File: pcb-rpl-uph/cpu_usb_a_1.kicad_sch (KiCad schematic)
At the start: 1 part, among them U5 RPL_UPH_FCBGA1744

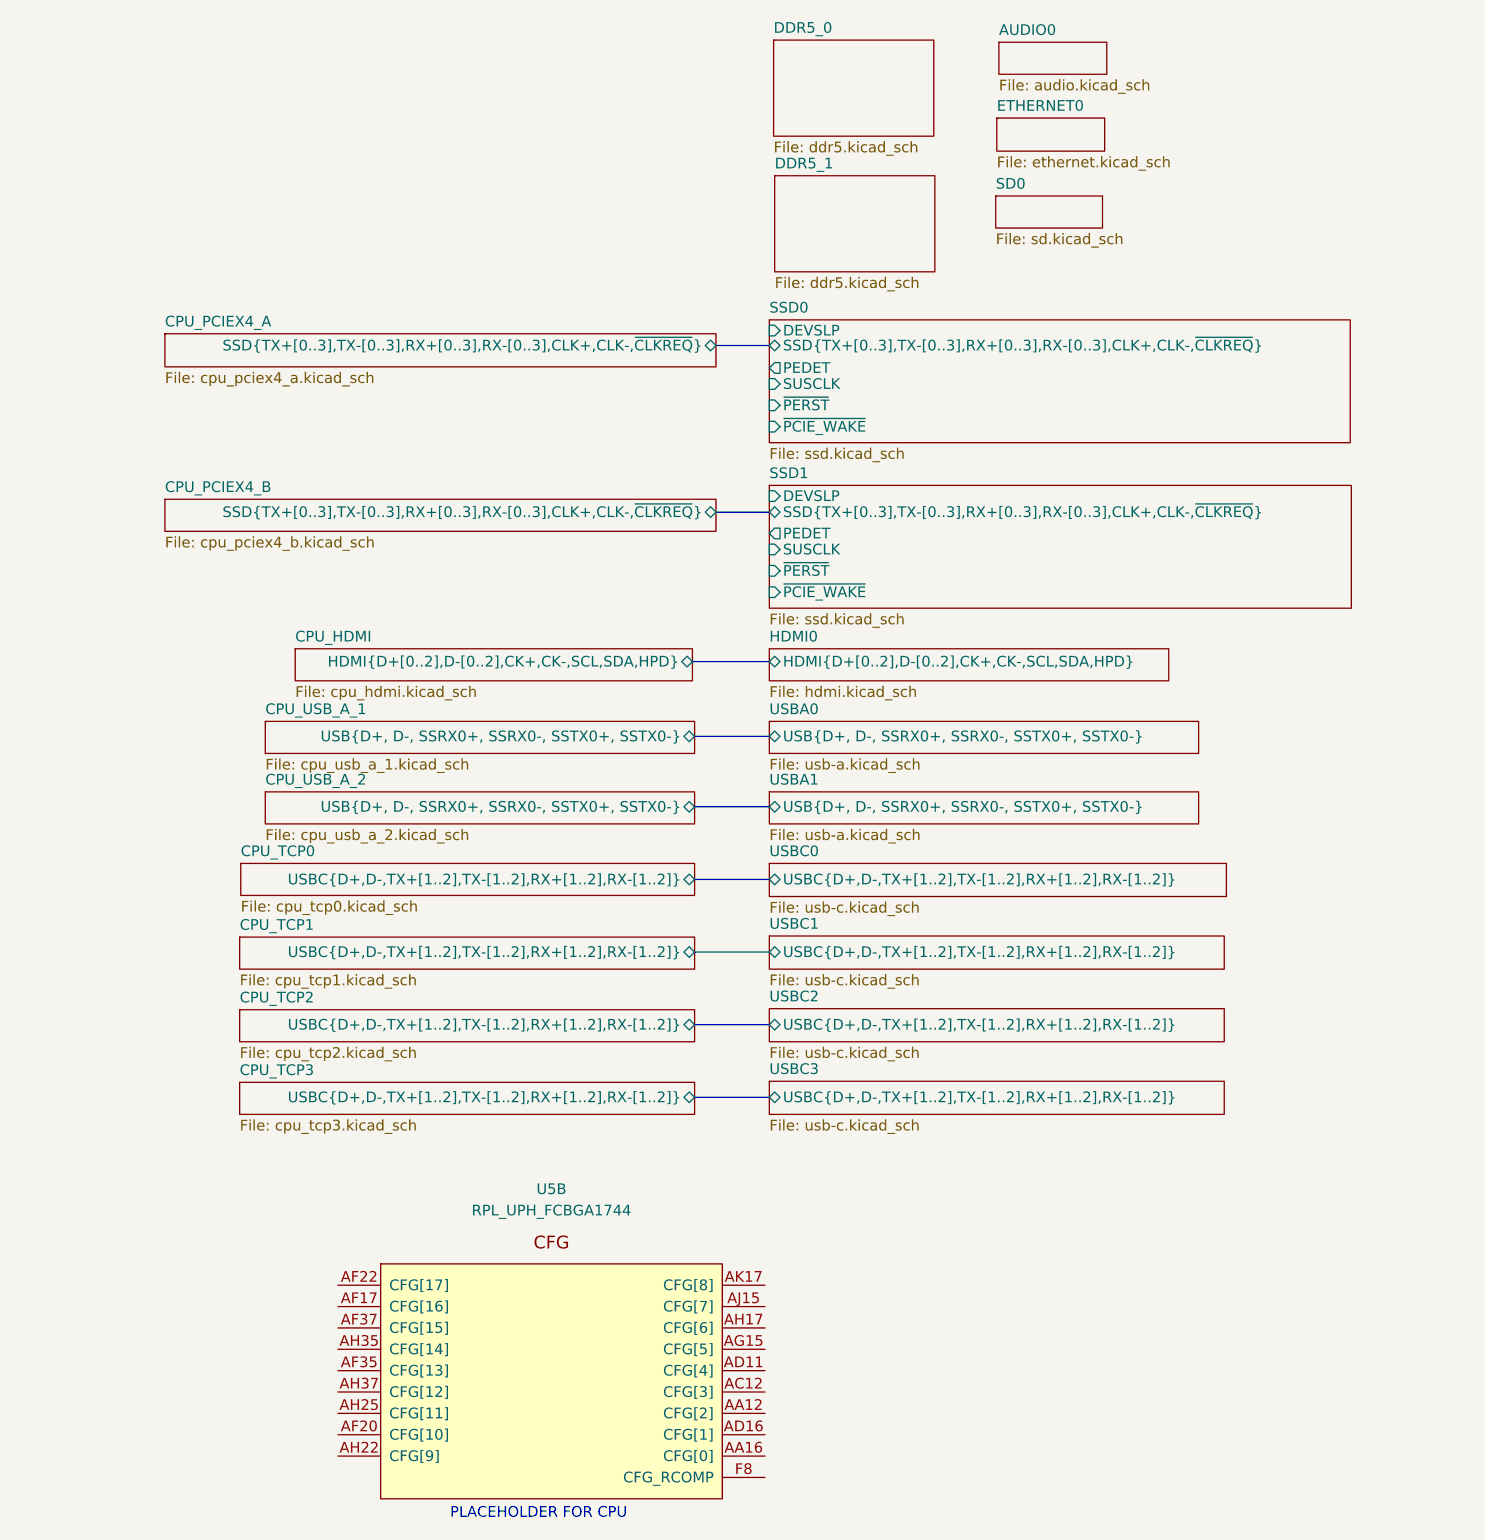
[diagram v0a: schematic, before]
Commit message: Connect USB-A and USB-C data
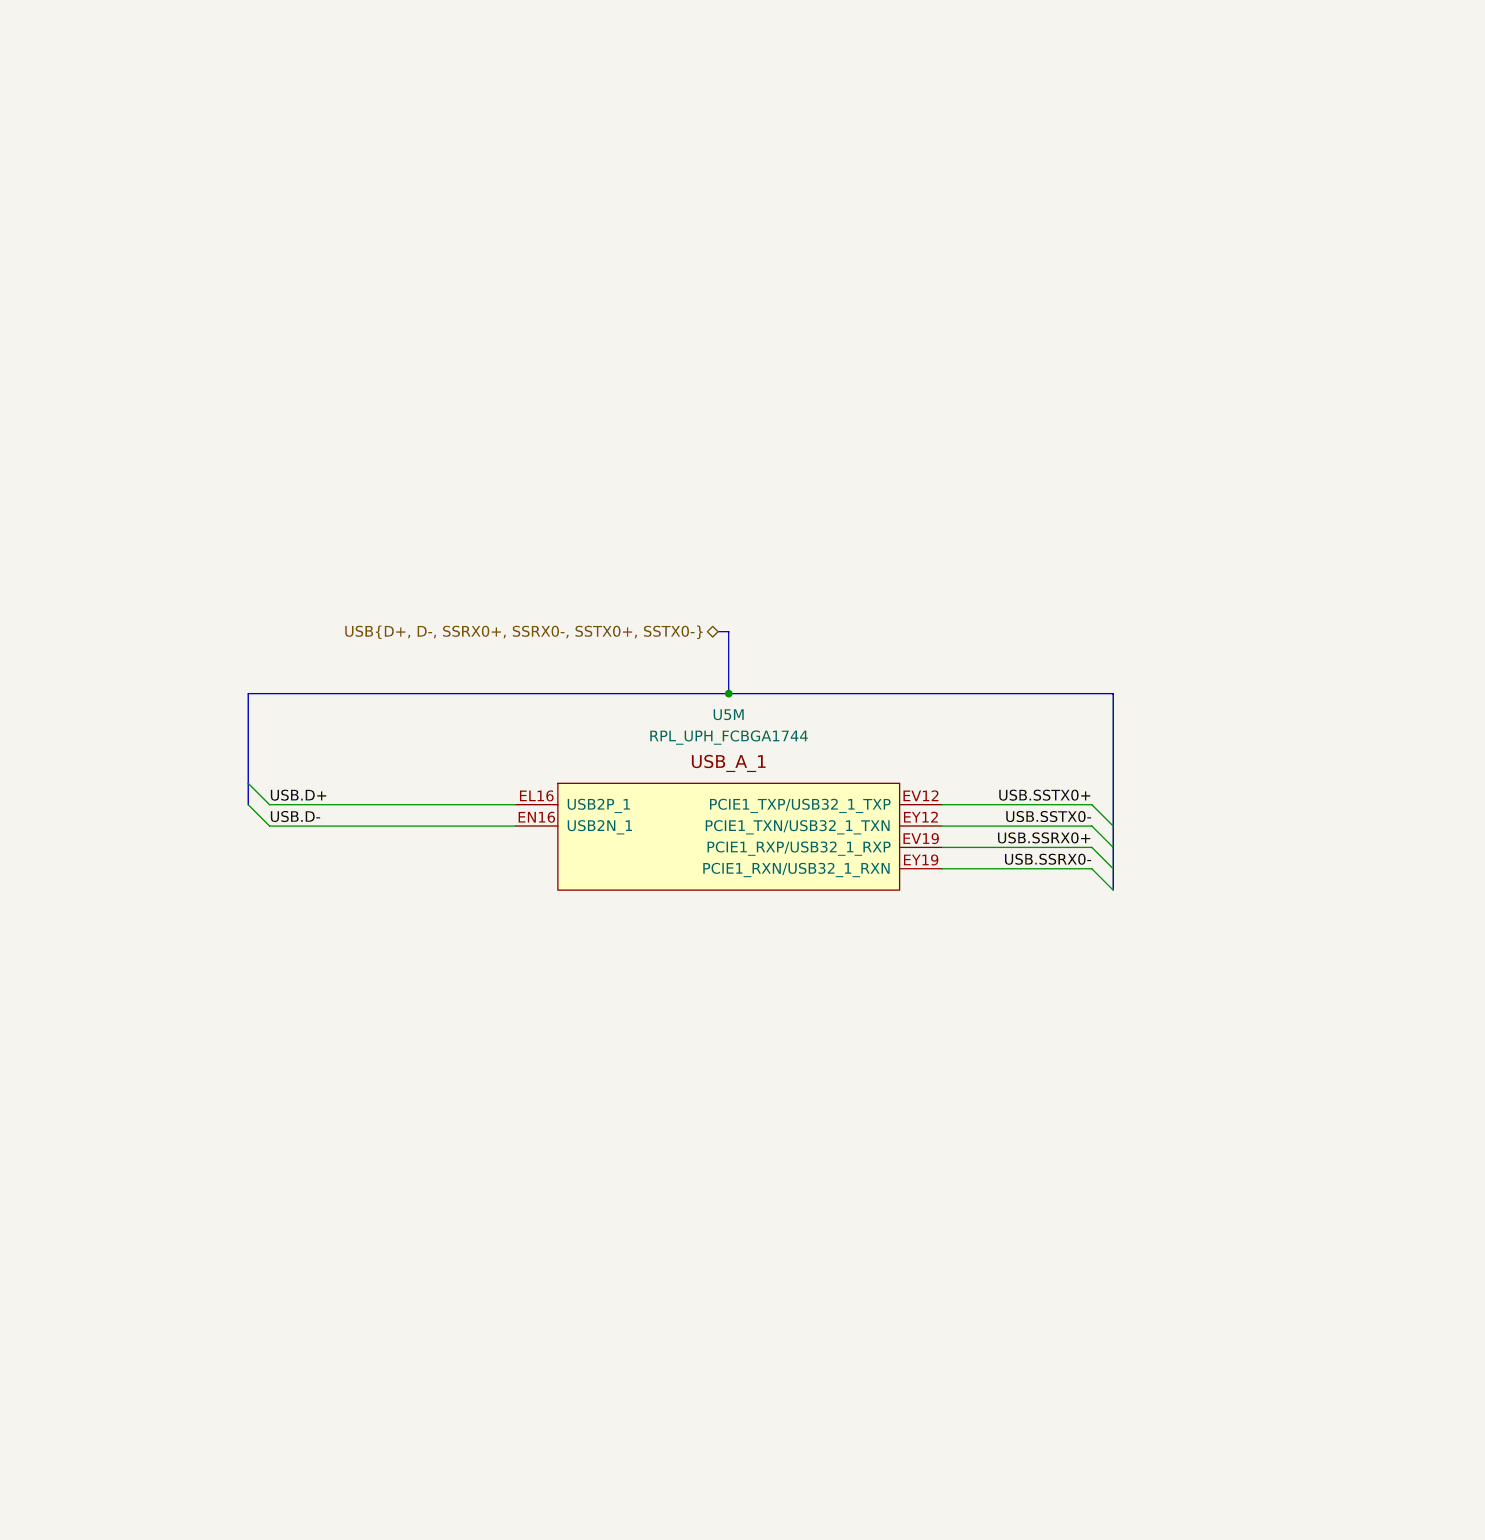
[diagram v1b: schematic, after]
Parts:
- removed U5: RPL_UPH_FCBGA1744, local:RPL_UPH_FCBGA1744, symbol local:RPL_UPH_FCBGA1744
- added U5: RPL_UPH_FCBGA1744, symbol local:RPL_UPH_FCBGA1744
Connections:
- new net USB.D+: U5.EL16 (USB2P_1)
- new net USB.D-: U5.EN16 (USB2N_1)
- new net USB.SSRX0+: U5.EV19 (PCIE1_RXP/USB32_1_RXP)
- new net USB.SSRX0-: U5.EY19 (PCIE1_RXN/USB32_1_RXN)
- new net USB.SSTX0+: U5.EV12 (PCIE1_TXP/USB32_1_TXP)
- new net USB.SSTX0-: U5.EY12 (PCIE1_TXN/USB32_1_TXN)
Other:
- removed sheet AUDIO0
- removed sheet CPU_HDMI
- removed sheet CPU_PCIEX4_A
- removed sheet CPU_PCIEX4_B
- removed sheet CPU_TCP0
- removed sheet CPU_TCP1
- removed sheet CPU_TCP2
- removed sheet CPU_TCP3
- removed sheet CPU_USB_A_1
- removed sheet CPU_USB_A_2
- removed sheet DDR5_0
- removed sheet DDR5_1
- removed sheet ETHERNET0
- removed sheet HDMI0
- removed sheet SD0
- removed sheet SSD0
- removed sheet SSD1
- removed sheet USBA0
- removed sheet USBA1
- removed sheet USBC0
- removed sheet USBC1
- removed sheet USBC2
- removed sheet USBC3
- note removed: "PLACEHOLDER FOR CPU"

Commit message: add display connector
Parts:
- U5: footprint (none) -> local:RPL_UPH_FCBGA1744
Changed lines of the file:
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@@
       (effects (font (size 1.27 1.27)))
     )
-    (property "Footprint" "" (at 137.414 100.838 0)
+    (property "Footprint" "local:RPL_UPH_FCBGA1744" (at 137.414 100.838 0)
       (effects (font (size 1.27 1.27)) hide)
     )
